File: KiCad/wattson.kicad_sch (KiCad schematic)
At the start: 23 parts, among them SW1 Keypad 1, SW10 Plug, SW11 On/Off, SW2 Keypad 2, SW3 Keypad 3, SW4 Keypad 4, SW5 Keypad 5, SW6 Keypad 0, SW7 Keypad 6, SW8 Keypad 7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

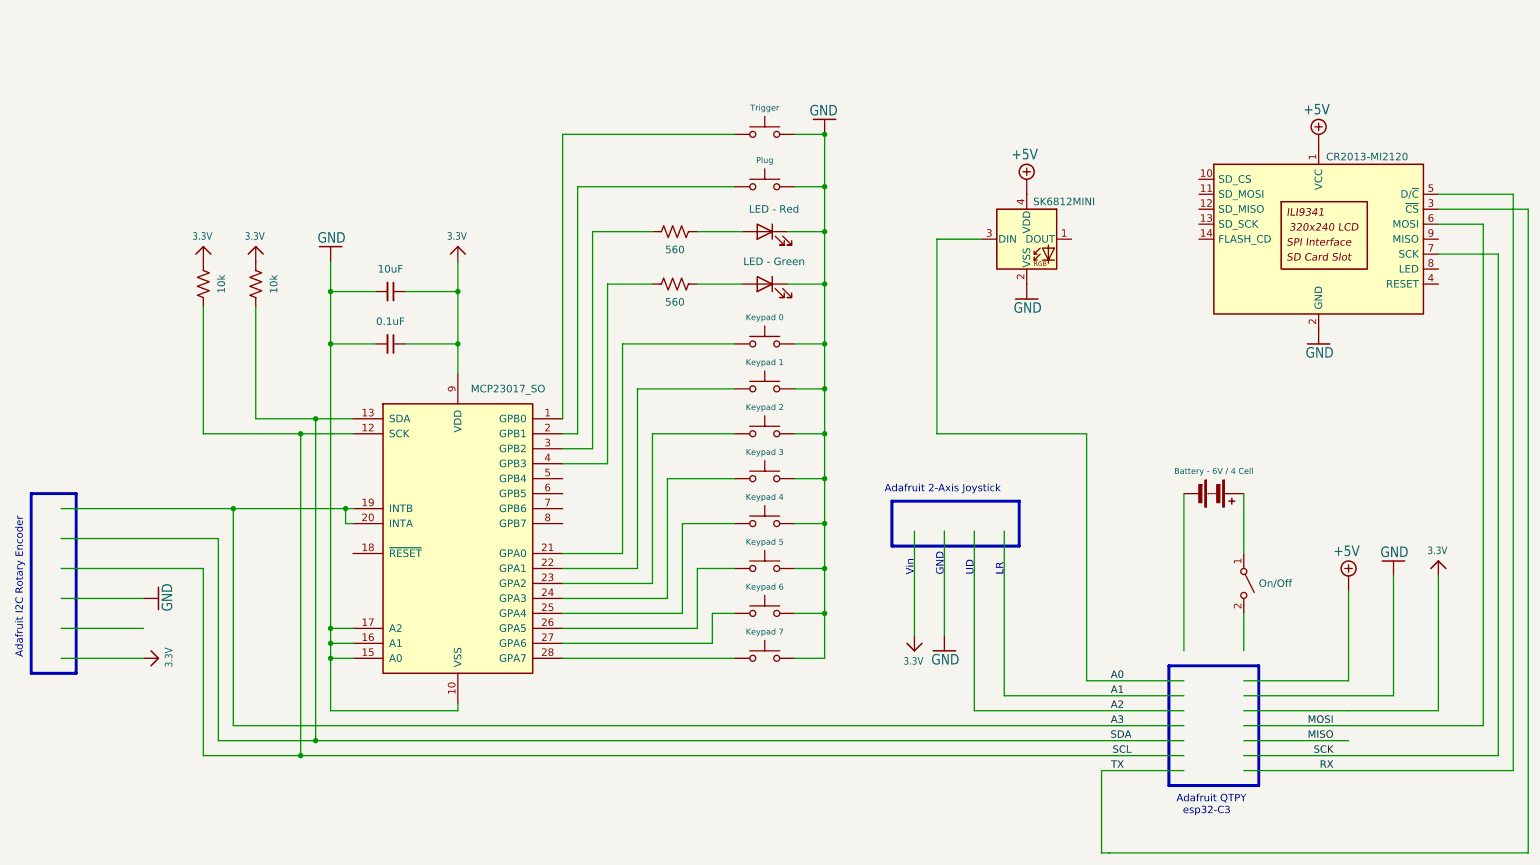
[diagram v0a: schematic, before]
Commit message: updates for neopixel and screen brightness
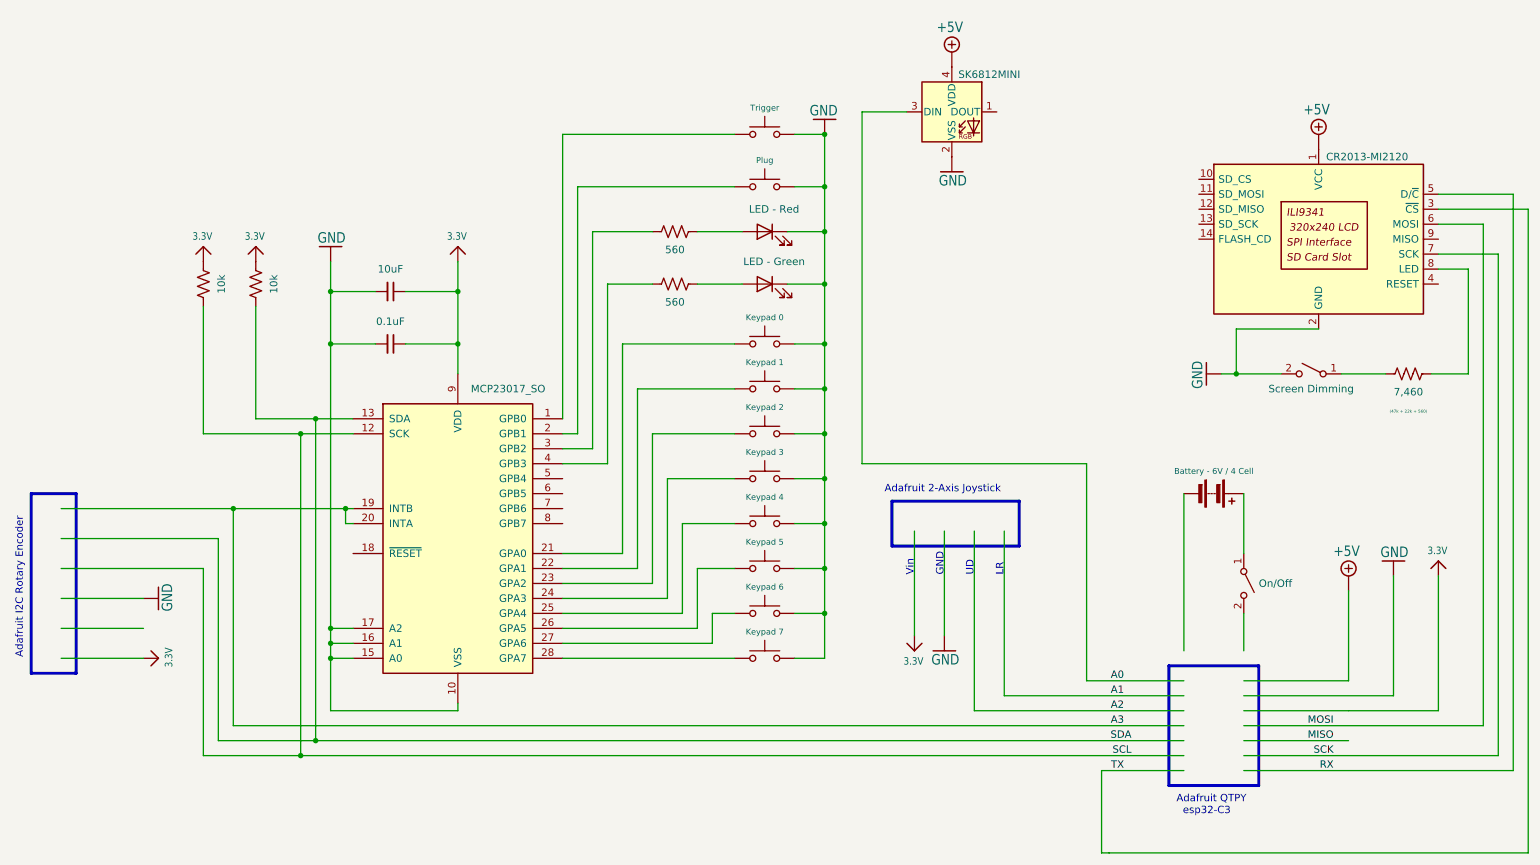
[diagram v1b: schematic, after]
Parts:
- added R5: 7,460, symbol Device:R_US
- added SW12: Screen Dimming, symbol Switch:SW_SPST
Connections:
- net GND: now also SW12.2 (B)
- net at U1.8 (LED): now also R5.1
- new net: R5.2, SW12.1 (A)
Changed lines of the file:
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@@
   (junction (at 71.12 116.84) (diameter 0) (color 0 0 0 0)
   )
+  (junction (at 224.79 73.66) (diameter 0) (color 0 0 0 0)
+  )
   (junction (at 71.12 121.92) (diameter 0) (color 0 0 0 0)
   )
@@
     (stroke (width 0) (type default))
   )
+  (wire (pts (xy 259.08 55.88) (xy 264.16 55.88))
+    (stroke (width 0) (type default))
+  )
   (wire (pts (xy 83.82 68.58) (xy 92.71 68.58))
     (stroke (width 0) (type default))
@@
     (stroke (width 0) (type default))
   )
-  (wire (pts (xy 173.99 83.82) (xy 173.99 50.8))
+  (wire (pts (xy 238.76 66.04) (xy 224.79 66.04))
+    (stroke (width 0) (type default))
+  )
+  (wire (pts (xy 161.29 88.9) (xy 161.29 29.21))
     (stroke (width 0) (type default))
   )
@@
     (stroke (width 0) (type default))
   )
-  (wire (pts (xy 199.39 125.73) (xy 199.39 83.82))
+  (wire (pts (xy 199.39 125.73) (xy 199.39 88.9))
     (stroke (width 0) (type default))
   )
@@
     (stroke (width 0) (type default))
   )
+  (wire (pts (xy 264.16 55.88) (xy 264.16 73.66))
+    (stroke (width 0) (type default))
+  )
   (wire (pts (xy 54.61 96.52) (xy 73.66 96.52))
     (stroke (width 0) (type default))
@@
     (stroke (width 0) (type default))
   )
+  (wire (pts (xy 224.79 66.04) (xy 224.79 73.66))
+    (stroke (width 0) (type default))
+  )
   (wire (pts (xy 71.12 130.81) (xy 92.71 130.81))
     (stroke (width 0) (type default))
@@
     (stroke (width 0) (type default))
   )
+  (wire (pts (xy 222.25 73.66) (xy 224.79 73.66))
+    (stroke (width 0) (type default))
+  )
   (wire (pts (xy 25.4 121.92) (xy 39.37 121.92))
     (stroke (width 0) (type default))
@@
     (stroke (width 0) (type default))
   )
+  (wire (pts (xy 224.79 73.66) (xy 232.41 73.66))
+    (stroke (width 0) (type default))
+  )
   (wire (pts (xy 226.06 138.43) (xy 269.24 138.43))
     (stroke (width 0.1524) (type solid))
@@
     (stroke (width 0) (type default))
   )
-  (wire (pts (xy 173.99 50.8) (xy 181.61 50.8))
+  (wire (pts (xy 161.29 29.21) (xy 168.91 29.21))
     (stroke (width 0) (type default))
   )
@@
     (stroke (width 0) (type default))
   )
+  (wire (pts (xy 264.16 73.66) (xy 257.81 73.66))
+    (stroke (width 0) (type default))
+  )
   (wire (pts (xy 74.93 99.06) (xy 73.66 99.06))
     (stroke (width 0) (type default))
@@
     (stroke (width 0) (type default))
   )
-  (wire (pts (xy 199.39 83.82) (xy 173.99 83.82))
+  (wire (pts (xy 199.39 88.9) (xy 161.29 88.9))
     (stroke (width 0) (type default))
   )
@@
   )
   (wire (pts (xy 118.11 58.42) (xy 118.11 88.9))
+    (stroke (width 0) (type default))
+  )
+  (wire (pts (xy 242.57 73.66) (xy 250.19 73.66))
     (stroke (width 0) (type default))
   )
@@
     )
   )
-  (symbol (lib_id "LED:SK6812MINI") (at 189.23 50.8 0) (unit 1)
-    (in_bom yes) (on_board yes) (dnp no)
-    (property "Reference" "D1" (at 201.93 47.1521 0)
-      (effects (font (size 1.27 1.27)) hide)
-    )
-    (property "Value" "SK6812MINI" (at 195.58 44.45 0)
+  (symbol (lib_id "LED:SK6812MINI") (at 176.53 29.21 0) (unit 1)
+    (in_bom yes) (on_board yes) (dnp no)
+    (property "Reference" "D1" (at 189.23 25.5621 0)
+      (effects (font (size 1.27 1.27)) hide)
+    )
+    (property "Value" "SK6812MINI" (at 182.88 22.86 0)
       (effects (font (size 1.27 1.27)))
     )
-    (property "Footprint" "LED_SMD:LED_SK6812MINI_PLCC4_3.5x3.5mm_P1.75mm" (at 190.5 58.42 0)
+    (property "Footprint" "LED_SMD:LED_SK6812MINI_PLCC4_3.5x3.5mm_P1.75mm" (at 177.8 36.83 0)
       (effects (font (size 1.27 1.27)) (justify left top) hide)
     )
-    (property "Datasheet" "https://cdn-shop.adafruit.com/product-files/2686/SK6812MINI_REV.01-1-2.pdf" (at 191.77 60.325 0)
+    (property "Datasheet" "https://cdn-shop.adafruit.com/product-files/2686/SK6812MINI_REV.01-1-2.pdf" (at 179.07 38.735 0)
       (effects (font (size 1.27 1.27)) (justify left top) hide)
     )
@@
         (path "/eff6c10b-1292-455c-9802-f747f2a9f123"
           (reference "#GND02") (unit 1)
+        )
+      )
+    )
+  )
+  (symbol (lib_id "Device:R_US") (at 254 73.66 270) (unit 1)
+    (in_bom yes) (on_board yes) (dnp no)
+    (property "Reference" "R5" (at 254 80.01 90)
+      (effects (font (size 1.27 1.27)) hide)
+    )
+    (property "Value" "7,460" (at 254 77.47 90)
+      (effects (font (size 1.27 1.27)) (justify bottom))
+    )
+    (property "Footprint" "" (at 253.746 74.676 90)
+      (effects (font (size 1.27 1.27)) hide)
+    )
+    (property "Datasheet" "~" (at 254 73.66 0)
+      (effects (font (size 1.27 1.27)) hide)
+    )
+    (property "Pairs" "(47k + 22k + 560)" (at 254 80.01 90)
+      (effects (font (size 0.5 0.5) (color 0 132 132 1)))
+    )
+    (pin "1")
+    (pin "2")
+    (instances
+      (project "wattson"
+        (path "/eff6c10b-1292-455c-9802-f747f2a9f123"
+          (reference "R5") (unit 1)
         )
       )
@@
     )
   )
+  (symbol (lib_id "Switch:SW_SPST") (at 237.49 73.66 0) (mirror y) (unit 1)
+    (in_bom yes) (on_board yes) (dnp no)
+    (property "Reference" "SW12" (at 237.49 67.31 0)
+      (effects (font (size 1.27 1.27)) hide)
+    )
+    (property "Value" "Screen Dimming" (at 237.49 76.2 0)
+      (effects (font (size 1.27 1.27)))
+    )
+    (property "Footprint" "" (at 237.49 73.66 0)
+      (effects (font (size 1.27 1.27)) hide)
+    )
+    (property "Datasheet" "~" (at 237.49 73.66 0)
+      (effects (font (size 1.27 1.27)) hide)
+    )
+    (pin "1")
+    (pin "2")
+    (instances
+      (project "wattson"
+        (path "/eff6c10b-1292-455c-9802-f747f2a9f123"
+          (reference "SW12") (unit 1)
+        )
+      )
+    )
+  )
   (symbol (lib_id "Adafruit QT Py ESP32-C3-eagle-import:3.3V") (at 58.42 52.07 0) (mirror y) (unit 1)
     (in_bom yes) (on_board yes) (dnp no)
@@
     )
   )
-  (symbol (lib_id "Adafruit QT Py ESP32-C3-eagle-import:GND") (at 189.23 60.96 0) (mirror y) (unit 1)
-    (in_bom yes) (on_board yes) (dnp no)
-    (property "Reference" "#GND2" (at 189.23 60.96 0)
-      (effects (font (size 1.27 1.27)) hide)
-    )
-    (property "Value" "GND" (at 191.77 63.5 0)
+  (symbol (lib_id "Adafruit QT Py ESP32-C3-eagle-import:GND") (at 176.53 39.37 0) (mirror y) (unit 1)
+    (in_bom yes) (on_board yes) (dnp no)
+    (property "Reference" "#GND2" (at 176.53 39.37 0)
+      (effects (font (size 1.27 1.27)) hide)
+    )
+    (property "Value" "GND" (at 179.07 41.91 0)
       (effects (font (size 1.778 1.5113)) (justify left bottom))
     )
-    (property "Footprint" "" (at 189.23 60.96 0)
-      (effects (font (size 1.27 1.27)) hide)
-    )
-    (property "Datasheet" "" (at 189.23 60.96 0)
+    (property "Footprint" "" (at 176.53 39.37 0)
+      (effects (font (size 1.27 1.27)) hide)
+    )
+    (property "Datasheet" "" (at 176.53 39.37 0)
       (effects (font (size 1.27 1.27)) hide)
     )
@@
     )
   )
-  (symbol (lib_id "Adafruit QT Py ESP32-C3-eagle-import:+5V") (at 189.23 40.64 0) (mirror y) (unit 1)
-    (in_bom yes) (on_board yes) (dnp no)
-    (property "Reference" "#SUPPLY3" (at 189.23 40.64 0)
-      (effects (font (size 1.27 1.27)) hide)
-    )
-    (property "Value" "+5V" (at 191.135 37.465 0)
+  (symbol (lib_id "Adafruit QT Py ESP32-C3-eagle-import:+5V") (at 176.53 19.05 0) (mirror y) (unit 1)
+    (in_bom yes) (on_board yes) (dnp no)
+    (property "Reference" "#SUPPLY3" (at 176.53 19.05 0)
+      (effects (font (size 1.27 1.27)) hide)
+    )
+    (property "Value" "+5V" (at 178.435 15.875 0)
       (effects (font (size 1.778 1.5113)) (justify left bottom))
     )
-    (property "Footprint" "" (at 189.23 40.64 0)
-      (effects (font (size 1.27 1.27)) hide)
-    )
-    (property "Datasheet" "" (at 189.23 40.64 0)
+    (property "Footprint" "" (at 176.53 19.05 0)
+      (effects (font (size 1.27 1.27)) hide)
+    )
+    (property "Datasheet" "" (at 176.53 19.05 0)
       (effects (font (size 1.27 1.27)) hide)
     )
@@
     )
   )
-  (symbol (lib_id "Adafruit QT Py ESP32-C3-eagle-import:GND") (at 238.76 68.58 0) (mirror y) (unit 1)
-    (in_bom yes) (on_board yes) (dnp no)
-    (property "Reference" "#GND2" (at 238.76 68.58 0)
-      (effects (font (size 1.27 1.27)) hide)
-    )
-    (property "Value" "GND" (at 241.3 71.12 0)
+  (symbol (lib_id "Adafruit QT Py ESP32-C3-eagle-import:GND") (at 219.71 73.66 270) (mirror x) (unit 1)
+    (in_bom yes) (on_board yes) (dnp no)
+    (property "Reference" "#GND2" (at 219.71 73.66 0)
+      (effects (font (size 1.27 1.27)) hide)
+    )
+    (property "Value" "GND" (at 217.17 76.2 0)
       (effects (font (size 1.778 1.5113)) (justify left bottom))
     )
-    (property "Footprint" "" (at 238.76 68.58 0)
-      (effects (font (size 1.27 1.27)) hide)
-    )
-    (property "Datasheet" "" (at 238.76 68.58 0)
-      (effects (font (size 1.27 1.27)) hide)
-    )
+    (property "Footprint" "" (at 219.71 73.66 0)
+      (effects (font (size 1.27 1.27)) hide)
+    )
+    (property "Datasheet" "" (at 219.71 73.66 0)
+      (effects (font (size 1.27 1.27)) hide)
+    )

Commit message: add screen brightness control
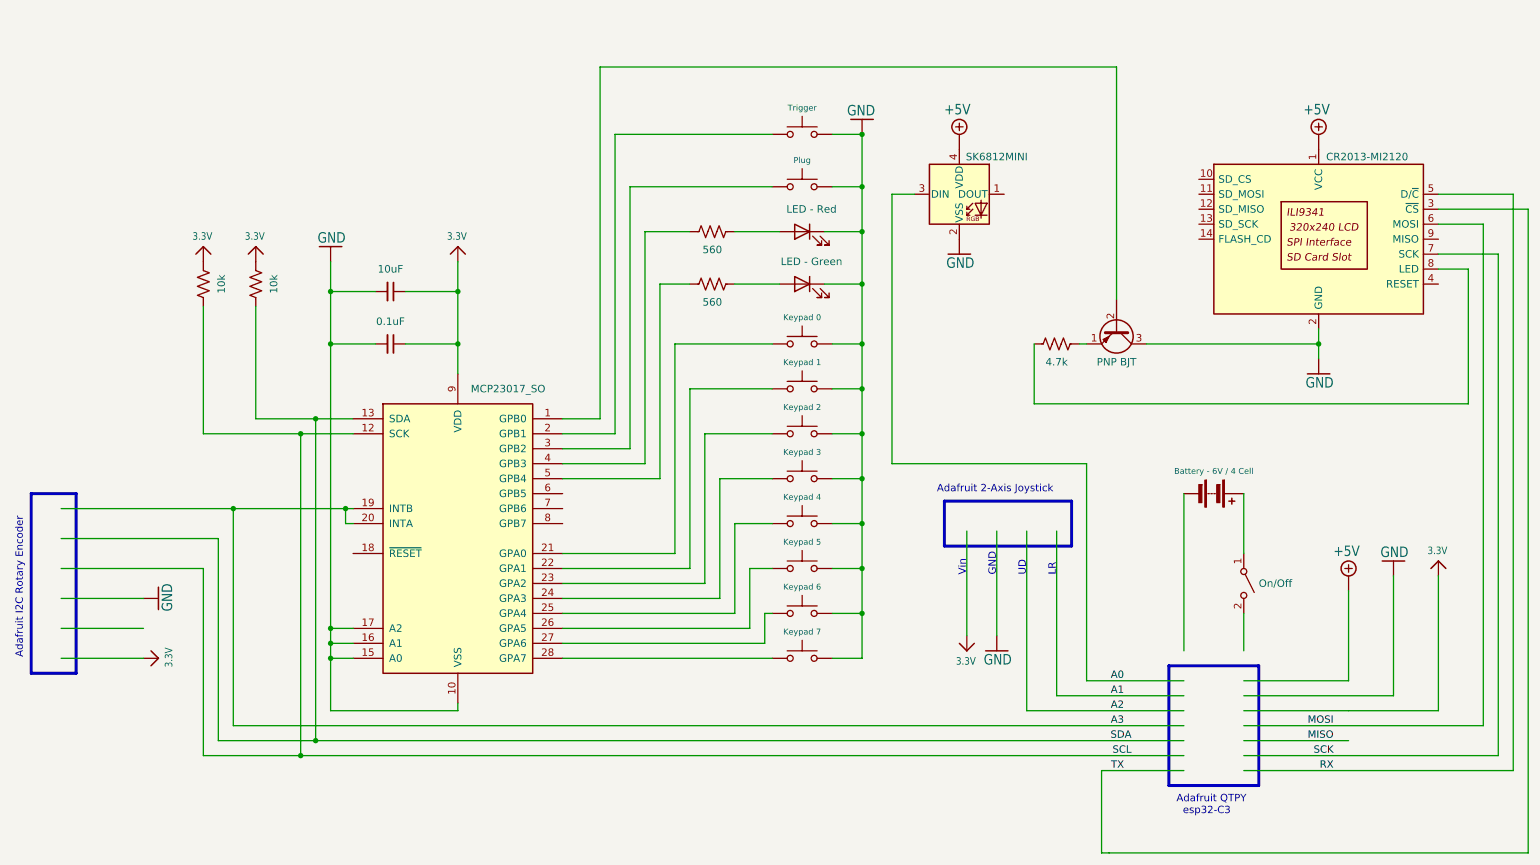
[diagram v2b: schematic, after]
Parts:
- removed SW12: Screen Dimming, symbol Switch:SW_SPST
- added Q1: PNP BJT, Package_TO_SOT_THT:TO-39-3, symbol Transistor_BJT:BC161
- R5: value 7,460 -> 4.7k; Pairs (47k + 22k + 560) -> (none)
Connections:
- net GND: now also Q1.3 (C)
- net at R5.1: now also Q1.1 (E); no longer U1.8 (LED)
- net at R5.2: now also U1.8 (LED)
- net at U2.1 (GPB0): now also Q1.2 (B); no longer SW9.1
- net at U2.2 (GPB1): now also SW9.1; no longer SW10.1
- net at U2.3 (GPB2): now also SW10.1; no longer R3.2
- net at U2.4 (GPB3): now also R3.2; no longer R4.2
- net at U2.5 (GPB4): now also R4.2

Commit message: start state, handle interrupts, init event loop
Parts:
- removed Q1: PNP BJT, Package_TO_SOT_THT:TO-39-3, symbol Transistor_BJT:BC161
- removed R5: 4.7k, symbol Device:R_US
- added R6: 7,460, symbol Device:R_US
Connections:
- net at U1.8 (LED): now also R6.2
- net at U2.1 (GPB0): now also R6.1
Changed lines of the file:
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@@
   (junction (at 161.29 114.3) (diameter 0) (color 0 0 0 0)
   )
-  (junction (at 238.76 68.58) (diameter 0) (color 0 0 0 0)
-  )
   (junction (at 161.29 91.44) (diameter 0) (color 0 0 0 0)
   )
@@
     (stroke (width 0) (type default))
   )
-  (wire (pts (xy 209.55 68.58) (xy 238.76 68.58))
-    (stroke (width 0) (type default))
-  )
   (wire (pts (xy 110.49 109.22) (xy 134.62 109.22))
     (stroke (width 0) (type default))
@@
     (stroke (width 0) (type default))
   )
+  (wire (pts (xy 204.47 78.74) (xy 204.47 68.58))
+    (stroke (width 0) (type default))
+  )
   (wire (pts (xy 116.84 81.28) (xy 110.49 81.28))
     (stroke (width 0) (type default))
@@
     (stroke (width 0) (type default))
   )
-  (wire (pts (xy 190.5 68.58) (xy 190.5 78.74))
-    (stroke (width 0) (type default))
-  )
   (wire (pts (xy 226.06 140.97) (xy 271.78 140.97))
     (stroke (width 0.1524) (type solid))
@@
     (stroke (width 0) (type default))
   )
-  (wire (pts (xy 190.5 78.74) (xy 264.16 78.74))
-    (stroke (width 0) (type default))
-  )
   (wire (pts (xy 58.42 81.28) (xy 68.58 81.28))
     (stroke (width 0) (type default))
   )
-  (wire (pts (xy 198.12 68.58) (xy 199.39 68.58))
+  (wire (pts (xy 264.16 78.74) (xy 204.47 78.74))
     (stroke (width 0) (type default))
   )
@@
     (stroke (width 0) (type default))
   )
-  (wire (pts (xy 238.76 68.58) (xy 238.76 71.12))
+  (wire (pts (xy 238.76 66.04) (xy 238.76 71.12))
     (stroke (width 0) (type default))
   )
@@
   )
   (wire (pts (xy 199.39 88.9) (xy 166.37 88.9))
-    (stroke (width 0) (type default))
-  )
-  (wire (pts (xy 238.76 66.04) (xy 238.76 68.58))
     (stroke (width 0) (type default))
   )
@@
         (path "/eff6c10b-1292-455c-9802-f747f2a9f123"
           (reference "#GND02") (unit 1)
-        )
-      )
-    )
-  )
-  (symbol (lib_id "Device:R_US") (at 194.31 68.58 270) (unit 1)
-    (in_bom yes) (on_board yes) (dnp no)
-    (property "Reference" "R5" (at 194.31 74.93 90)
-      (effects (font (size 1.27 1.27)) hide)
-    )
-    (property "Value" "4.7k" (at 194.31 72.39 90)
-      (effects (font (size 1.27 1.27)) (justify bottom))
-    )
-    (property "Footprint" "" (at 194.056 69.596 90)
-      (effects (font (size 1.27 1.27)) hide)
-    )
-    (property "Datasheet" "~" (at 194.31 68.58 0)
-      (effects (font (size 1.27 1.27)) hide)
-    )
-    (pin "1")
-    (pin "2")
-    (instances
-      (project "wattson"
-        (path "/eff6c10b-1292-455c-9802-f747f2a9f123"
-          (reference "R5") (unit 1)
-        )
-      )
-    )
-  )
-  (symbol (lib_id "Transistor_BJT:BC161") (at 204.47 66.04 270) (unit 1)
-    (in_bom yes) (on_board yes) (dnp no)
-    (property "Reference" "Q1" (at 204.47 72.39 90)
-      (effects (font (size 1.27 1.27)) hide)
-    )
-    (property "Value" "PNP BJT" (at 204.47 72.39 90)
-      (effects (font (size 1.27 1.27)) (justify bottom))
-    )
-    (property "Footprint" "Package_TO_SOT_THT:TO-39-3" (at 202.565 71.12 0)
-      (effects (font (size 1.27 1.27) italic) (justify left) hide)
-    )
-    (property "Datasheet" "http://www.farnell.com/datasheets/1697389.pdf" (at 204.47 66.04 0)
-      (effects (font (size 1.27 1.27)) (justify left) hide)
-    )
-    (pin "1")
-    (pin "2")
-    (pin "3")
-    (instances
-      (project "wattson"
-        (path "/eff6c10b-1292-455c-9802-f747f2a9f123"
-          (reference "Q1") (unit 1)
         )
       )
@@
         )
       )
+    )
+  )
+  (symbol (lib_id "Device:R_US") (at 204.47 64.77 0) (unit 1)
+    (in_bom yes) (on_board yes) (dnp no)
+    (property "Reference" "R6" (at 210.82 64.77 90)
+      (effects (font (size 1.27 1.27)) hide)
+    )
+    (property "Value" "7,460" (at 208.28 64.77 90)
+      (effects (font (size 1.27 1.27)) (justify bottom))
+    )
+    (property "Footprint" "" (at 205.486 65.024 90)
+      (effects (font (size 1.27 1.27)) hide)
+    )
+    (property "Datasheet" "~" (at 204.47 64.77 0)
+      (effects (font (size 1.27 1.27)) hide)
+    )
+    (property "Pairs" "(47k + 2.2k + 560)" (at 210.82 64.77 90)
+      (effects (font (size 0.5 0.5) (color 0 132 132 1)))
+    )
+    (pin "1")
+    (pin "2")
+    (instances
+      (project "wattson"
+        (path "/eff6c10b-1292-455c-9802-f747f2a9f123"
+          (reference "R6") (unit 1)
+        )
+      )
